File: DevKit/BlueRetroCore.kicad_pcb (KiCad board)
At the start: 4 copper layers, 85 x 56 mm, 108 parts, among them J1 USB_C_Receptacle_USB2.0, J2 Conn_02x06, J3 Micro_SD_Card, J4 Conn_01x03, J5 DB25_Female_MountingHoles, J6 Conn_02x13, J7 Conn_02x07, Q1 BSS138, Q2 BSS138, Q3 S8050, Q4 S8050, Q5 S8050, SW1 BOOT, SW2 EN, U1 ESP32-WROOM, U10 TPD6F003, U11 TPD6F003, U12 TPD6F003, U13 TPD6F003, U2 FT2232HL, U3 STL6N3LLH6, U4 TCPP01-M12, U5 M93C46, U6 ECMF02-2AMX6, U7 TPD6F003, U8 AP7361C-33E, U9 AP7361C-33E, Y1 12MHz

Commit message: PCB routing
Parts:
- removed R29, R30: 0, BlueRetro:R_0603_1608Metric
- H1, H2, H3, H4: footprint BlueRetro:MountingHole_3.2mm_M3 -> BlueRetro:MountingHole_2.7mm_M2.5
- U1: value ESP32-WROOM -> ESP32-WROOM-32E
- U8, U9: footprint BlueRetro:SOT-223-3_TabPin2 -> BlueRetro:SOT-223-3_TabPin3
- moved R19 23.5 mm to (-23.2, -26.5), turned to 270 degrees
- moved D8 23.5 mm to (26.8, -23.4), turned to 90 degrees
- moved R20 22.8 mm to (-25.7, -26.5), turned to 270 degrees
- moved R22 22.6 mm to (-30.8, -26.5), turned to 270 degrees
- moved R21 22.4 mm to (-28.3, -26.5), turned to 270 degrees
- moved C24 19.7 mm to (28.2, 16.5)
- moved U12 18.2 mm to (19.1, 7.65)
- moved U8 18.0 mm to (25.7, 22.9), turned to 270 degrees
- moved U13 17.7 mm to (19.1, 10.8)
- moved C25 17.5 mm to (21.1, 18.8)
- moved D7 14.9 mm to (-16.5, 27.0)
- moved R27 14.8 mm to (-13.7, 27.0), turned to 180 degrees
- moved C27 13.4 mm to (-22.0, 21.2), turned to 270 degrees
- moved D9 12.8 mm to (16.5, 14.5), turned to 180 degrees
- moved R14 12.6 mm to (-24.2, 26.7), turned to 0 degrees
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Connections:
- net Net-(J1-PadA6) renamed /USB_C_P
- net Net-(J1-PadA7) renamed /USB_C_N
- net Net-(U2-Pad7) renamed /USB_N
- net Net-(U2-Pad8) renamed /USB_P
- J1 pad A8: (no net) -> Net-(J1-PadA8)
- J1 pad B8: (no net) -> Net-(J1-PadB8)
- J3 pad 10: (no net) -> Net-(J3-Pad10)
- J3 pad 9: (no net) -> Net-(J3-Pad9)
- J5 pad 1: /IO19_C -> /IO23_C
- J5 pad 10: /IO32_C -> /I34_C
- J5 pad 11: /IO33_C -> /IO32_C
- J5 pad 12: /I34_C -> /IO25_C
- J5 pad 13: /I35_C -> /IO27_C
- J5 pad 14: /IO0_C -> /IO22_C
- J5 pad 15: /IO1_C -> /IO3_C
- J5 pad 16: /IO3_C -> /IO19_C
- J5 pad 18: /IO16_C -> /IO17_C
- J5 pad 19: /IO17_C -> /IO16_C
- J5 pad 2: /IO21_C -> /IO1_C
- J5 pad 20: /IO18_C -> /IO0_C
- J5 pad 21: /IO23_C -> /I36_C
- J5 pad 22: /IO26_C -> /I39_C
- J5 pad 23: /IO27_C -> /I35_C
- J5 pad 24: /I36_C -> /IO33_C
- J5 pad 25: /I39_C -> /IO26_C
- J5 pad 3: /IO22_C -> /IO21_C
- J5 pad 4: /IO25_C -> /IO18_C
- J6 pad 1: /IO19_C -> /IO23_C
- J6 pad 10: /IO32_C -> /I34_C
- J6 pad 11: /IO33_C -> /IO32_C
- J6 pad 12: /I34_C -> /IO25_C
- J6 pad 13: /I35_C -> /IO27_C
- J6 pad 14: /IO0_C -> /IO22_C
- J6 pad 15: /IO1_C -> /IO3_C
- J6 pad 16: /IO3_C -> /IO19_C
- J6 pad 18: /IO16_C -> /IO17_C
- J6 pad 19: /IO17_C -> /IO16_C
- J6 pad 2: /IO21_C -> /IO1_C
- J6 pad 20: /IO18_C -> /IO0_C
- J6 pad 21: /IO23_C -> /I36_C
- J6 pad 22: /IO26_C -> /I39_C
- J6 pad 23: /IO27_C -> /I35_C
- J6 pad 24: /I36_C -> /IO33_C
- J6 pad 25: /I39_C -> /IO26_C
- J6 pad 3: /IO22_C -> /IO21_C
- J6 pad 4: /IO25_C -> /IO18_C
- J7 pad 10: /TMS -> /TCK
- J7 pad 11: /EN -> /IO12
- J7 pad 12: /nTRST -> /TDI
- J7 pad 3: /IO13 -> /EN
- J7 pad 4: /TCK -> /nTRST
- J7 pad 5: /IO12 -> /IO14
- J7 pad 6: /TDI -> /TMS
- J7 pad 9: /IO14 -> /IO13
- U1 pad 17: (no net) -> Net-(U1-Pad17)
- U1 pad 18: (no net) -> Net-(U1-Pad18)
- U1 pad 19: (no net) -> Net-(U1-Pad19)
- U1 pad 20: (no net) -> Net-(U1-Pad20)
- U1 pad 21: (no net) -> Net-(U1-Pad21)
- U1 pad 22: (no net) -> Net-(U1-Pad22)
- U1 pad 32: (no net) -> Net-(U1-Pad32)
- U10 pad 1: /IO19 -> /IO23
- U10 pad 10: /IO21_C -> /IO1_C
- U10 pad 11: /IO0_C -> /IO22_C
- U10 pad 12: /IO19_C -> /IO23_C
- U10 pad 2: /IO0 -> /IO22
- U10 pad 3: /IO21 -> /IO1
- U10 pad 4: /IO1 -> /IO3
- U10 pad 5: /IO22 -> /IO21
- U10 pad 6: /IO3 -> /IO19
- U10 pad 7: /IO3_C -> /IO19_C
- U10 pad 8: /IO22_C -> /IO21_C
- U10 pad 9: /IO1_C -> /IO3_C
- U11 pad 1: /IO25 -> /IO18
- U11 pad 10: /IO16_C -> /IO17_C
- U11 pad 12: /IO25_C -> /IO18_C
- U11 pad 3: /IO16 -> /IO17
- U11 pad 4: /IO17 -> /IO16
- U11 pad 5: /IO18 -> /IO0
- U11 pad 6: /IO23 -> /I36
- U11 pad 7: /IO23_C -> /I36_C
- U11 pad 8: /IO18_C -> /IO0_C
- U11 pad 9: /IO17_C -> /IO16_C
- U12 pad 1: /IO26 -> /I39
- U12 pad 10: /IO27_C -> /I35_C
- U12 pad 11: /IO32_C -> /I34_C
- U12 pad 12: /IO26_C -> /I39_C
- U12 pad 2: /IO32 -> /I34
- U12 pad 3: /IO27 -> /I35
- U12 pad 4: /IO33 -> /IO32
- U12 pad 5: /I36 -> /IO33
- U12 pad 6: /I34 -> /IO25
- U12 pad 7: /I34_C -> /IO25_C
- U12 pad 8: /I36_C -> /IO33_C
- U12 pad 9: /IO33_C -> /IO32_C
- U13 pad 1: /I39 -> /IO26
- U13 pad 10: (no net) -> Net-(U13-Pad10)
- U13 pad 11: /I35_C -> /IO27_C
- U13 pad 12: /I39_C -> /IO26_C
- U13 pad 2: /I35 -> /IO27
- U13 pad 3: (no net) -> Net-(U13-Pad3)
- U13 pad 4: (no net) -> Net-(U13-Pad4)
- U13 pad 5: (no net) -> Net-(U13-Pad5)
- U13 pad 6: (no net) -> Net-(U13-Pad6)
- U13 pad 7: (no net) -> Net-(U13-Pad7)
- U13 pad 8: (no net) -> Net-(U13-Pad8)
- U13 pad 9: (no net) -> Net-(U13-Pad9)
- U2 pad 21: (no net) -> Net-(U2-Pad21)
- U2 pad 23: (no net) -> Net-(U2-Pad23)
- U2 pad 24: (no net) -> Net-(U2-Pad24)
- U2 pad 26: (no net) -> Net-(U2-Pad26)
- U2 pad 27: (no net) -> Net-(U2-Pad27)
- U2 pad 28: (no net) -> Net-(U2-Pad28)
- U2 pad 29: (no net) -> Net-(U2-Pad29)
- U2 pad 30: (no net) -> Net-(U2-Pad30)
- U2 pad 32: (no net) -> Net-(U2-Pad32)
- U2 pad 33: (no net) -> Net-(U2-Pad33)
- U2 pad 34: (no net) -> Net-(U2-Pad34)
- U2 pad 36: (no net) -> Net-(U2-Pad36)
- U2 pad 44: (no net) -> Net-(U2-Pad44)
- U2 pad 45: (no net) -> Net-(U2-Pad45)
- U2 pad 46: (no net) -> Net-(U2-Pad46)
- U2 pad 48: (no net) -> Net-(U2-Pad48)
- U2 pad 52: (no net) -> Net-(U2-Pad52)
- U2 pad 53: (no net) -> Net-(U2-Pad53)
- U2 pad 57: (no net) -> Net-(U2-Pad57)
- U2 pad 58: (no net) -> Net-(U2-Pad58)
- U2 pad 59: (no net) -> Net-(U2-Pad59)
- U2 pad 60: (no net) -> Net-(U2-Pad60)
- U3 pad 1: Net-(D1-Pad2) -> Net-(D2-Pad1)
- U3 pad 2: Net-(D1-Pad2) -> Net-(D2-Pad1)
- U3 pad 3: Net-(D1-Pad2) -> Net-(U3-Pad3)
- U3 pad 4: Net-(U3-Pad4) -> Net-(D1-Pad2)
- U3 pad 8: Net-(D2-Pad1) -> Net-(D1-Pad2)
- U4 pad 5: Net-(U3-Pad4) -> Net-(U3-Pad3)
- U5 pad 6: (no net) -> Net-(U5-Pad6)
- U5 pad 7: (no net) -> Net-(U5-Pad7)
- U6 pad 4: (no net) -> Net-(U6-Pad4)
- U7 pad 1: /IO12 -> /IO4
- U7 pad 10: Net-(J3-Pad3) -> Net-(J3-Pad5)
- U7 pad 11: Net-(J3-Pad2) -> Net-(J3-Pad7)
- U7 pad 12: Net-(J3-Pad1) -> Net-(J3-Pad8)
- U7 pad 2: /IO13 -> /IO2
- U7 pad 3: /IO15 -> /IO14
- U7 pad 4: /IO14 -> /IO15
- U7 pad 5: /IO2 -> /IO13
- U7 pad 6: /IO4 -> /IO12
- U7 pad 7: Net-(J3-Pad8) -> Net-(J3-Pad1)
- U7 pad 8: Net-(J3-Pad7) -> Net-(J3-Pad2)
- U7 pad 9: Net-(J3-Pad5) -> Net-(J3-Pad3)
- U8 pad 2: Net-(R29-Pad1) -> GND
- U9 pad 2: Net-(R30-Pad1) -> GND
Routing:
- net /IO17: track 0.00 -> 100.0 mm, vias 0 -> 2
- net /IO2: track 0.00 -> 82.9 mm, vias 0 -> 3
- net +5V: track 0.00 -> 82.9 mm, vias 0 -> 2
- net /IO15: track 0.00 -> 81.1 mm, vias 0 -> 1
- net +3V3: track 0.00 -> 77.3 mm, vias 0 -> 8
- net /IO13: track 0.00 -> 73.9 mm, vias 0 -> 1
- net /EN: track 0.00 -> 68.8 mm, vias 0 -> 2
- net /IO12: track 0.00 -> 65.5 mm, vias 0 -> 1
- net /nRTS: track 0.00 -> 57.6 mm, vias 0 -> 2
- net /IO4: track 0.00 -> 56.6 mm, vias 0 -> 2
- net /IO14: track 0.00 -> 56.1 mm
- net /nDTR: track 0.00 -> 50.5 mm, vias 0 -> 4
- net VBUS: track 0.00 -> 49.0 mm
- net /VIN_C: track 0.00 -> 48.8 mm, vias 0 -> 1
- net /I39: track 0.00 -> 46.0 mm, vias 0 -> 2
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- added copper zone on F.Cu, net +1V8
- added copper zone on In2.Cu, net +3V3
- added copper zone on In2.Cu, net +3V3_USB
- added copper zone on B.Cu, net GND
- added copper zone on F.Cu, net GND
- added copper zone on In1.Cu, net GND
- added copper zone on F.Cu, net Net-(J1-PadS1)
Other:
- net class Default: clearance 0.2 -> 0.15; trace_width 0.25 -> 0.2
- rule trace_clearance: 0.2 -> 0.15
- rule trace_min: 0.2 -> 0.15

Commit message: Add logo
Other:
- board text added: "BlueRetro"
- board text added: "v1.0"

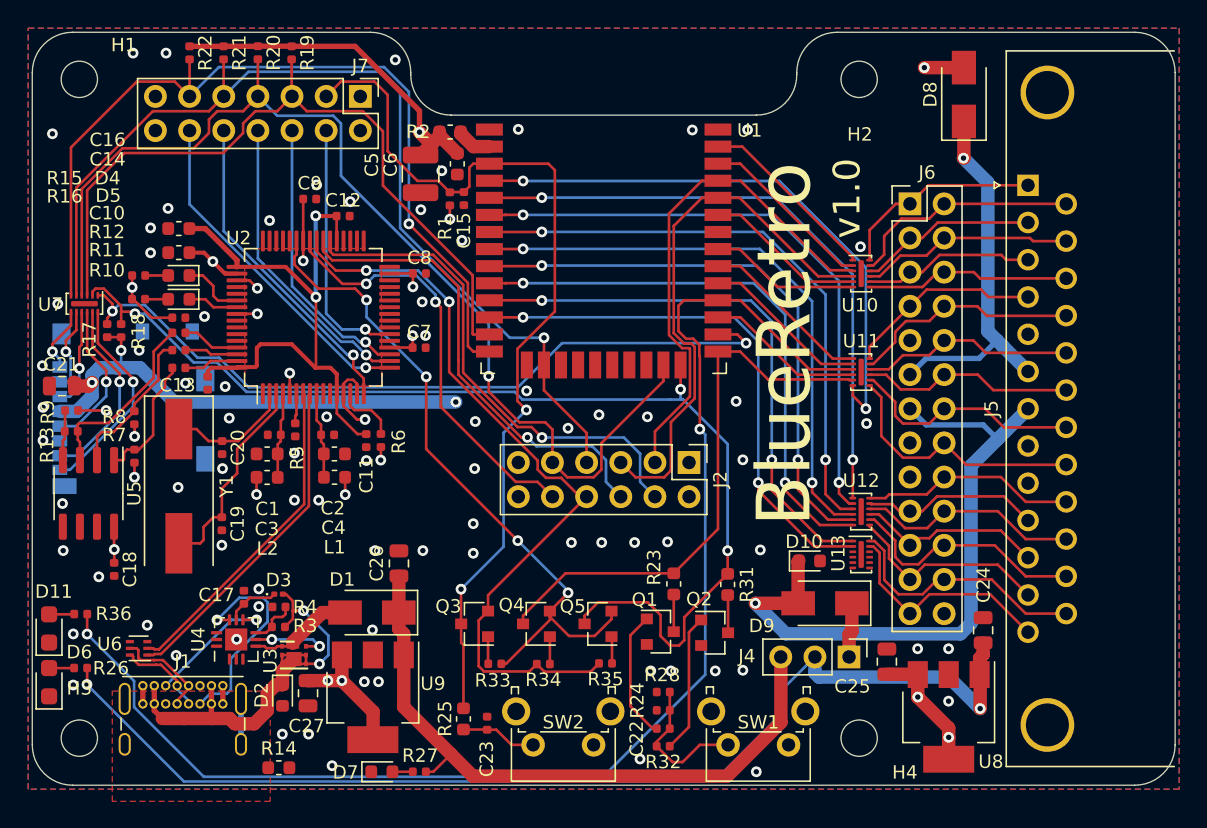
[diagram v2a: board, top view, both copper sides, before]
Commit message: Add 0.8mm pullback to board edge
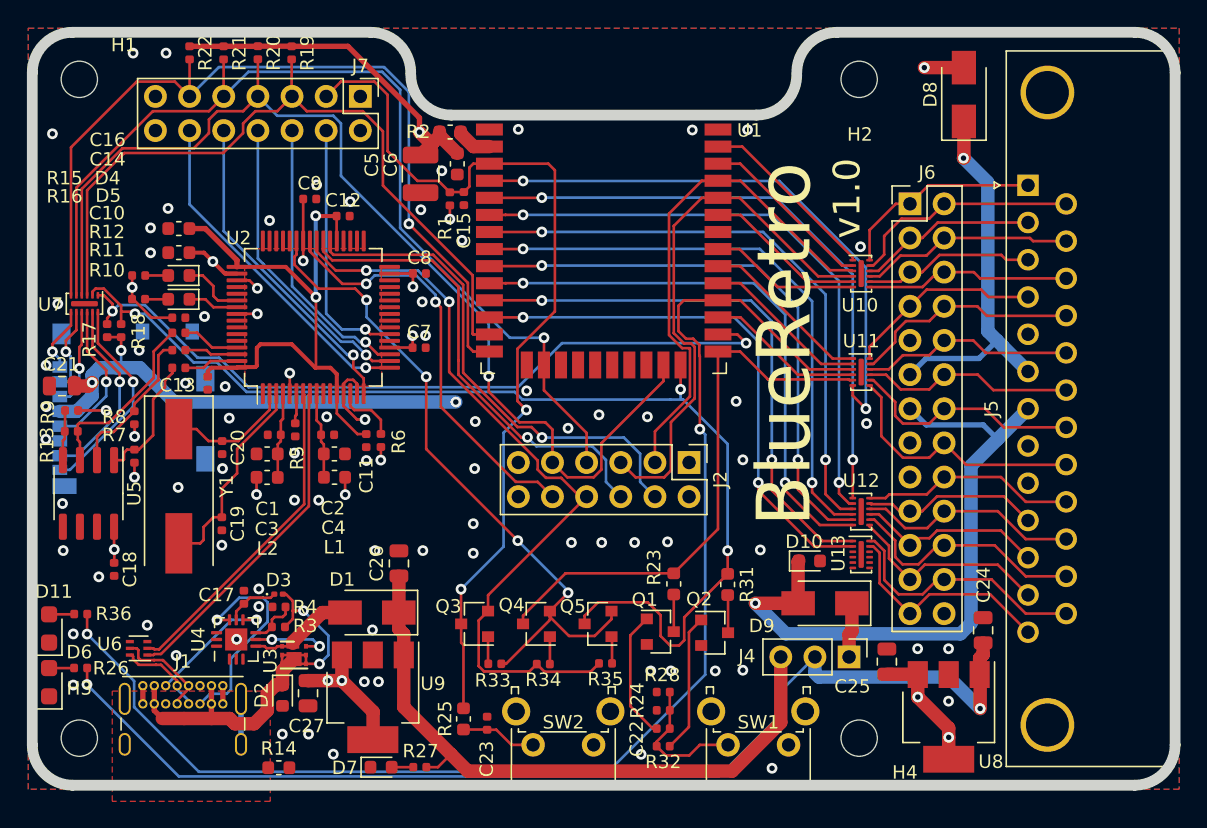
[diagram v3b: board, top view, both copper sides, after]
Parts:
- moved D7 0.34 mm to (-16.6, 26.7)
- moved R27 0.34 mm to (-13.7, 26.7)
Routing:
- net GND: vias 82 -> 81

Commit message: LED is on by default at boot and shutdown by software
This allow to detect bootloader/flash issue
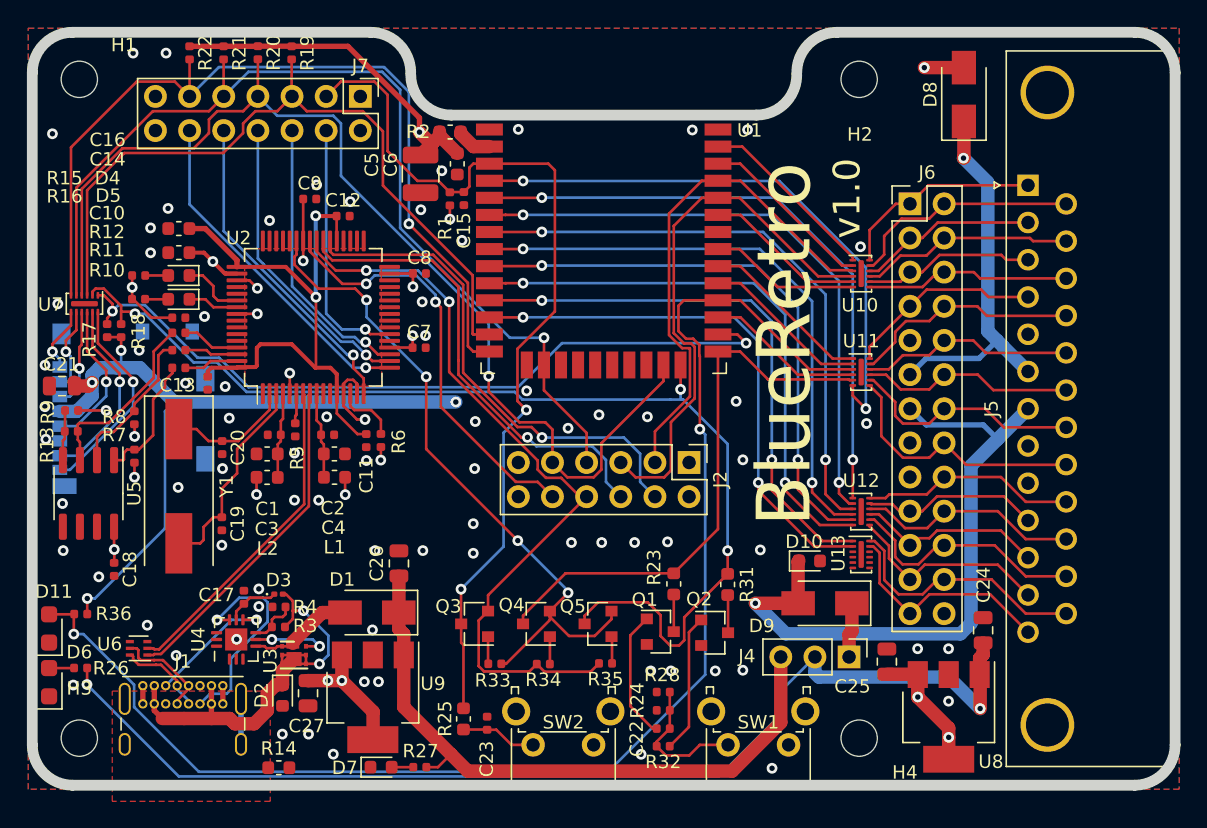
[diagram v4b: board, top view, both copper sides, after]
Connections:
- D11 pad 2: Net-(D11-Pad2) -> /IO17
- J1 pad A8: Net-(J1-PadA8) -> (no net)
- J1 pad B8: Net-(J1-PadB8) -> (no net)
- J3 pad 10: Net-(J3-Pad10) -> (no net)
- J3 pad 9: Net-(J3-Pad9) -> (no net)
- R36 pad 1: /IO17 -> +3V3
- R36 pad 2: Net-(D11-Pad2) -> /IO17
- U1 pad 17: Net-(U1-Pad17) -> (no net)
- U1 pad 18: Net-(U1-Pad18) -> (no net)
- U1 pad 19: Net-(U1-Pad19) -> (no net)
- U1 pad 20: Net-(U1-Pad20) -> (no net)
- U1 pad 21: Net-(U1-Pad21) -> (no net)
- U1 pad 22: Net-(U1-Pad22) -> (no net)
- U1 pad 32: Net-(U1-Pad32) -> (no net)
- U13 pad 10: Net-(U13-Pad10) -> (no net)
- U13 pad 3: Net-(U13-Pad3) -> (no net)
- U13 pad 4: Net-(U13-Pad4) -> (no net)
- U13 pad 5: Net-(U13-Pad5) -> (no net)
- U13 pad 6: Net-(U13-Pad6) -> (no net)
- U13 pad 7: Net-(U13-Pad7) -> (no net)
- U13 pad 8: Net-(U13-Pad8) -> (no net)
- U13 pad 9: Net-(U13-Pad9) -> (no net)
- U2 pad 21: Net-(U2-Pad21) -> (no net)
- U2 pad 23: Net-(U2-Pad23) -> (no net)
- U2 pad 24: Net-(U2-Pad24) -> (no net)
- U2 pad 26: Net-(U2-Pad26) -> (no net)
- U2 pad 27: Net-(U2-Pad27) -> (no net)
- U2 pad 28: Net-(U2-Pad28) -> (no net)
- U2 pad 29: Net-(U2-Pad29) -> (no net)
- U2 pad 30: Net-(U2-Pad30) -> (no net)
- U2 pad 32: Net-(U2-Pad32) -> (no net)
- U2 pad 33: Net-(U2-Pad33) -> (no net)
- U2 pad 34: Net-(U2-Pad34) -> (no net)
- U2 pad 36: Net-(U2-Pad36) -> (no net)
- U2 pad 44: Net-(U2-Pad44) -> (no net)
- U2 pad 45: Net-(U2-Pad45) -> (no net)
- U2 pad 46: Net-(U2-Pad46) -> (no net)
- U2 pad 48: Net-(U2-Pad48) -> (no net)
- U2 pad 52: Net-(U2-Pad52) -> (no net)
- U2 pad 53: Net-(U2-Pad53) -> (no net)
- U2 pad 57: Net-(U2-Pad57) -> (no net)
- U2 pad 58: Net-(U2-Pad58) -> (no net)
- U2 pad 59: Net-(U2-Pad59) -> (no net)
- U2 pad 60: Net-(U2-Pad60) -> (no net)
- U5 pad 6: Net-(U5-Pad6) -> (no net)
- U5 pad 7: Net-(U5-Pad7) -> (no net)
- U6 pad 4: Net-(U6-Pad4) -> (no net)
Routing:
- net +3V3: track 77.0 -> 95.8 mm, vias 8 -> 9
- net /IO17: track 99.7 -> 102.4 mm
- net Net-(D11-Pad2): track 1.88 -> 0.00 mm
- net Net-(U1-Pad32): track 0.83 -> 0.00 mm
- net GND: vias 81 -> 80

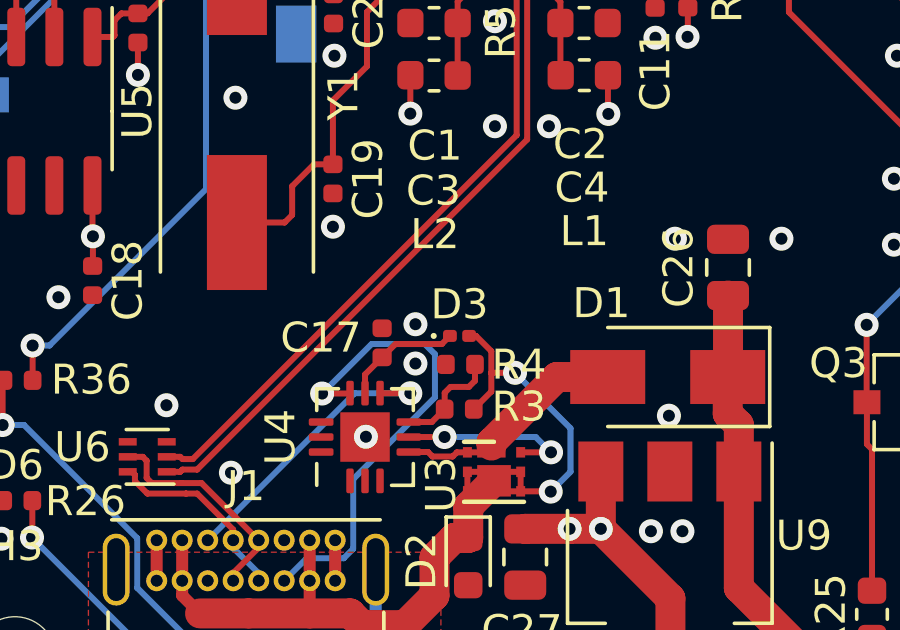
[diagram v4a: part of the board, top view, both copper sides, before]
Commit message: Replace D3 with a bigger alternative
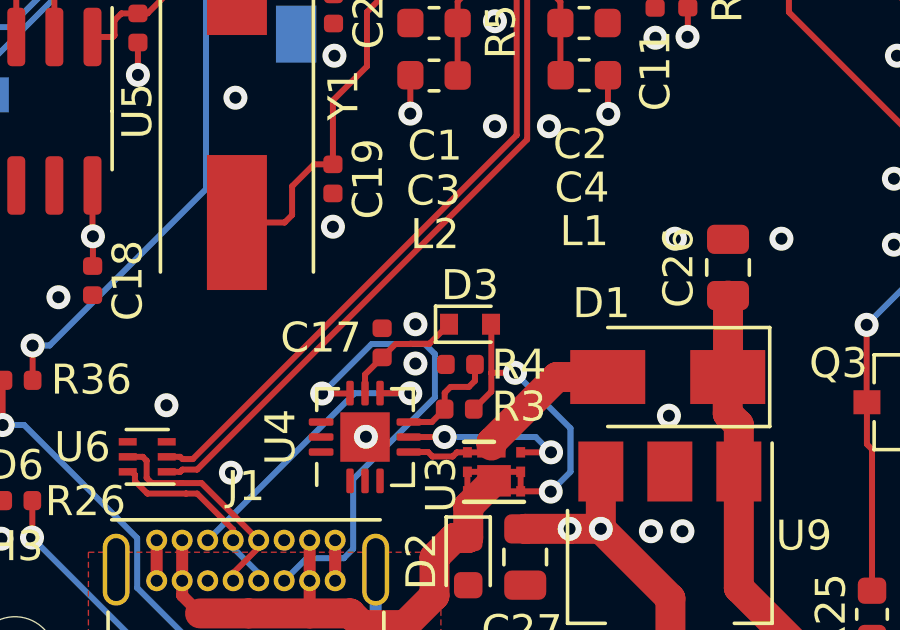
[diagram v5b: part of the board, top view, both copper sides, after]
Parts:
- D3: value BAT30F4 -> BAT54KFILM; footprint BlueRetro:D_0201_0603Metric -> BlueRetro:D_SOD-523
- J5: value DB25_Female_MountingHoles -> DB25_Female
- moved D3 0.52 mm to (-23.8, 13.4)

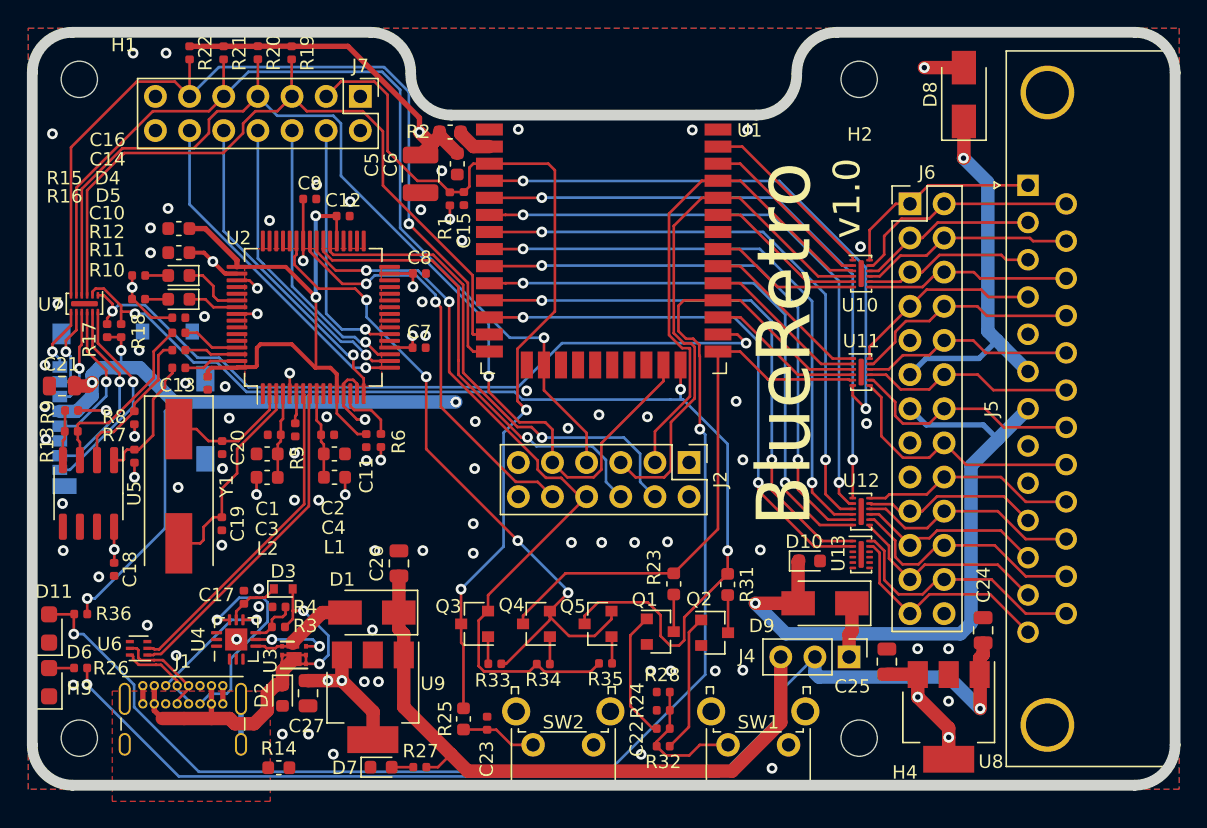
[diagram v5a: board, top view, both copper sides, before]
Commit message: Fix SOT-223 Tab
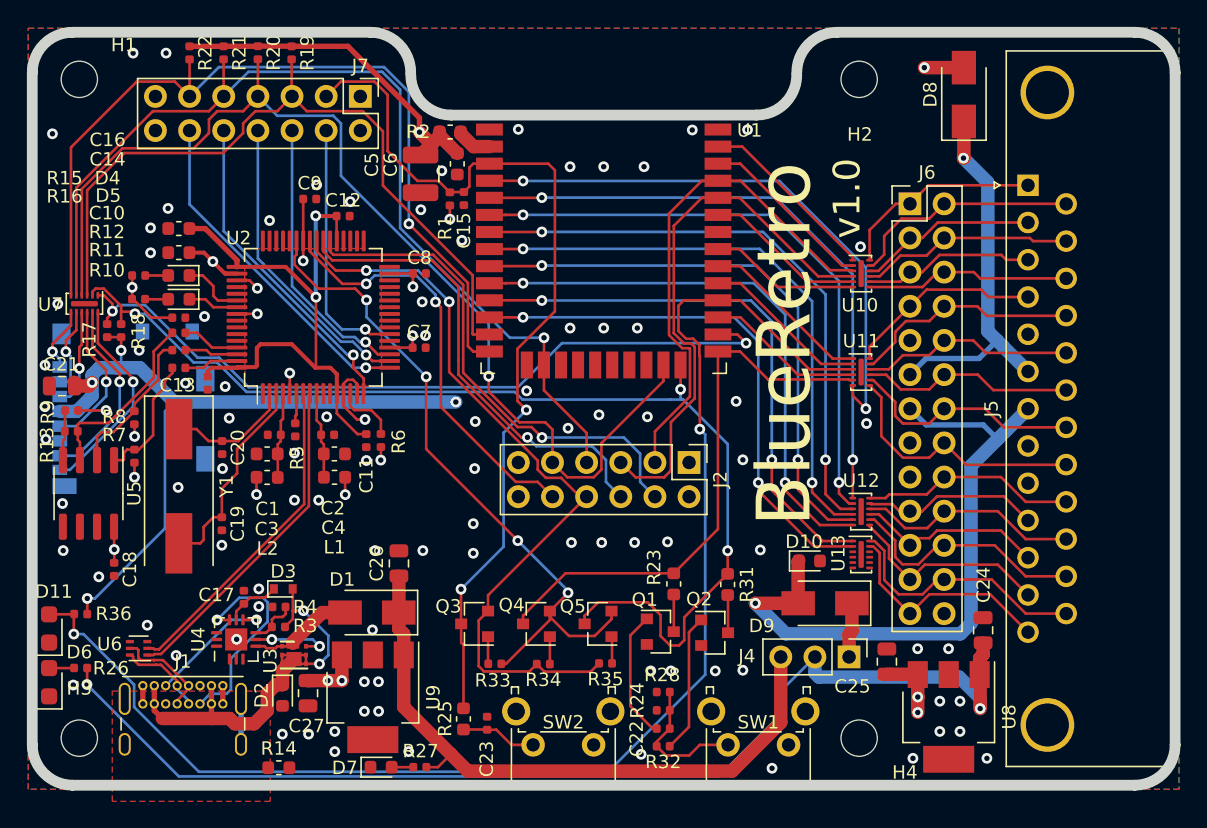
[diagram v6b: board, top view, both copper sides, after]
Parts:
- U8, U9: footprint BlueRetro:SOT-223-3_TabPin3 -> BlueRetro:SOT-223-3_TabPin2
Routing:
- net +3V3_USB: track 41.1 -> 35.8 mm
- net +3V3: track 95.8 -> 91.4 mm
- net GND: track 11.6 -> 11.7 mm, vias 80 -> 95
